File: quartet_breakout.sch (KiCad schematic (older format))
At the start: 1 part, among them J5 Conn_01x18

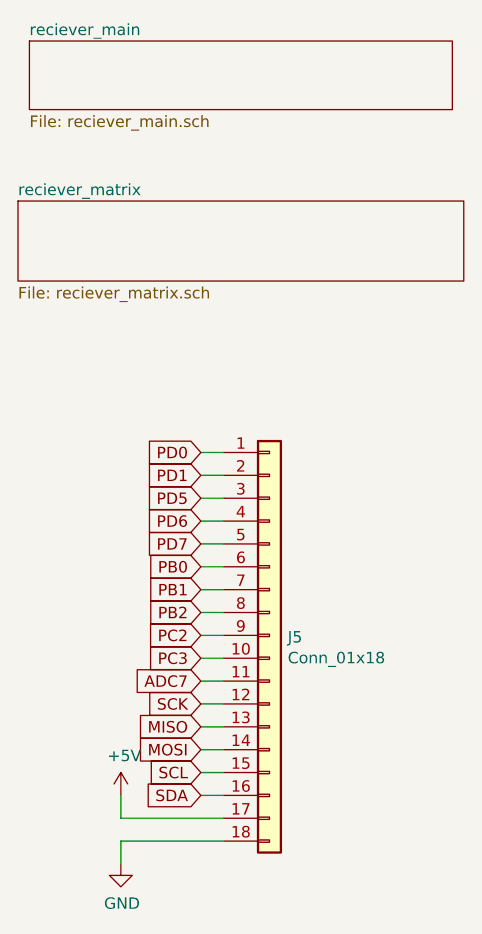
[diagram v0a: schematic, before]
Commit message: Reroute matrix, redo schematics for feather compat
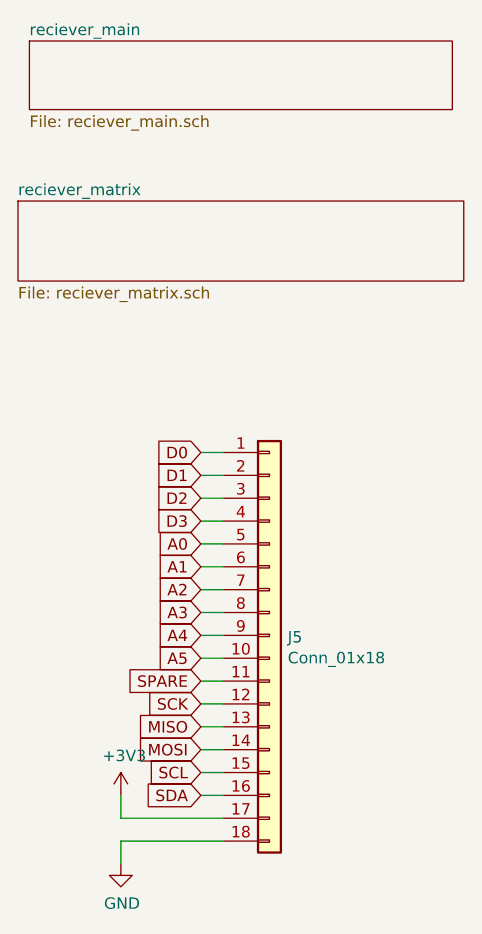
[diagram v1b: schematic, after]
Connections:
- net +5V renamed +3V3
- net ADC7 renamed SPARE
- net PB0 renamed A1
- net PB1 renamed A2
- net PB2 renamed A3
- net PC2 renamed A4
- net PC3 renamed A5
- net PD0 renamed D0
- net PD1 renamed D1
- net PD5 renamed D2
- net PD6 renamed D3
- net PD7 renamed A0
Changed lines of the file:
@@
 $EndComp
 Text GLabel 3300 4350 0    50   Input ~ 0
-PD1
+D1
 Text GLabel 3300 4250 0    50   Input ~ 0
-PD0
+D0
 Text GLabel 3300 4450 0    50   Input ~ 0
-PD5
+D2
 Text GLabel 3300 4550 0    50   Input ~ 0
-PD6
+D3
 Text GLabel 3300 4650 0    50   Input ~ 0
-PD7
+A0
 Text GLabel 3300 4750 0    50   Input ~ 0
-PB0
+A1
 Text GLabel 3300 4850 0    50   Input ~ 0
-PB1
+A2
 Text GLabel 3300 4950 0    50   Input ~ 0
-PB2
+A3
 Text GLabel 3300 5050 0    50   Input ~ 0
-PC2
+A4
 Text GLabel 3300 5150 0    50   Input ~ 0
-PC3
+A5
 Text GLabel 3300 5250 0    50   Input ~ 0
-ADC7
+SPARE
 Wire Wire Line
 	3300 5250 3400 5250
@@
 Wire Wire Line
 	2950 5950 2950 6050
+Wire Wire Line
+	2950 5850 3400 5850
+Wire Wire Line
+	2950 5950 3400 5950
 $Comp
-L power:+5V #PWR?
-U 1 1 5FF7CAD6
+L power:+3V3 #PWR?
+U 1 1 60477FB3
 P 2950 5750
-AR Path="/5FF53271/5FF7CAD6" Ref="#PWR?"  Part="1"
-AR Path="/5FF53271/5FF7CBCC/5FF7CAD6" Ref="#PWR?"  Part="1"
-AR Path="/5FF5604D/5FF9299E/5FF7CAD6" Ref="#PWR?"  Part="1"
-AR Path="/5FF77C9D/5FF7CAD6" Ref="#PWR?"  Part="1"
-AR Path="/5FF7CAD6" Ref="#PWR0101"  Part="1"
-F 0 "#PWR0101" H 2950 5600 50  0001 C CNN
-F 1 "+5V" H 2965 5923 50  0000 C CNN
+F 0 "#PWR?" H 2950 5600 50  0001 C CNN
+F 1 "+3V3" H 2965 5923 50  0000 C CNN
 F 2 "" H 2950 5750 50  0001 C CNN
 F 3 "" H 2950 5750 50  0001 C CNN
@@
 	1    0    0    -1
 $EndComp
-Wire Wire Line
-	2950 5850 3400 5850
-Wire Wire Line
-	2950 5950 3400 5950
 $EndSCHEMATC
